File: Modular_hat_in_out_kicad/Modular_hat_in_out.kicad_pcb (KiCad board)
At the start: 2 copper layers, 65 x 56 mm, 147 parts, among them J1 Raspberry_Pi_2_3, U1 MCP3008, U2 LM324, U3 MCP3008, U4 MCP4728, U5 MCP4728, U6 LM324

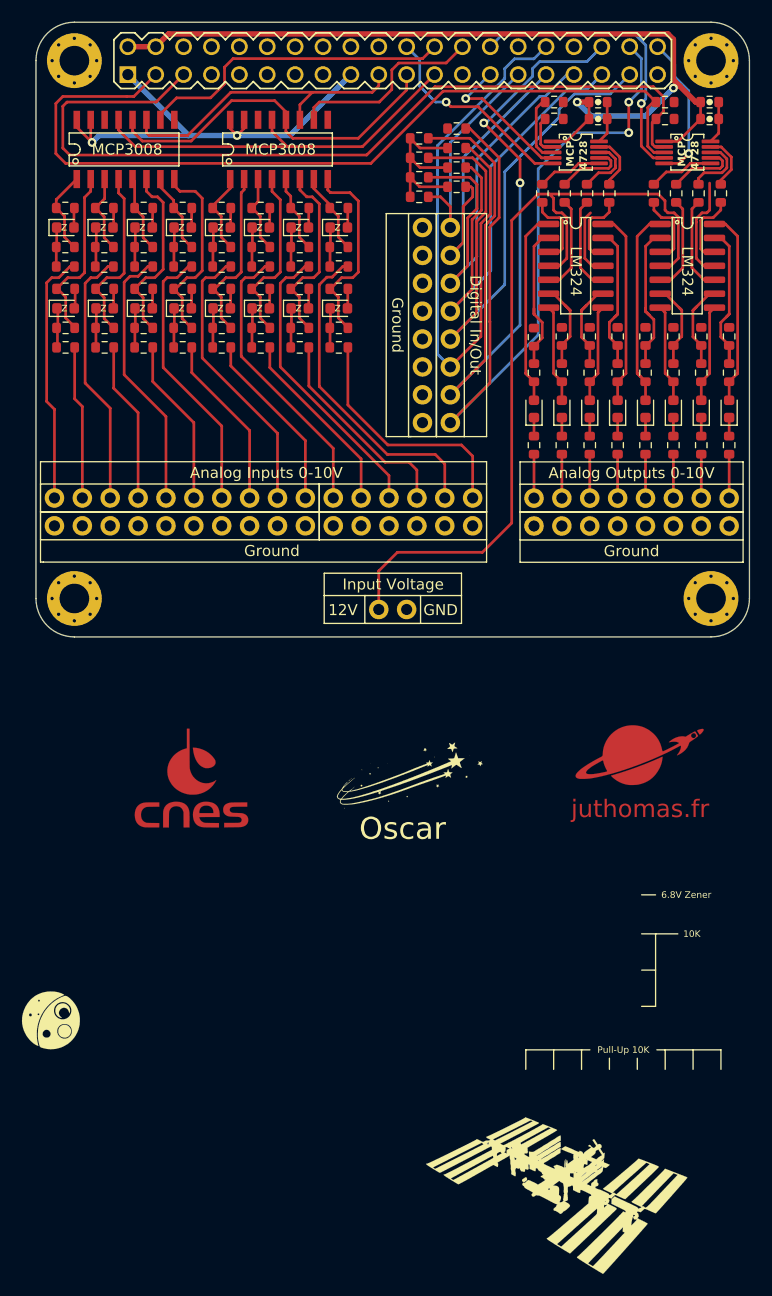
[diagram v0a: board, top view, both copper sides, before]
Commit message: [ADD] Some routing
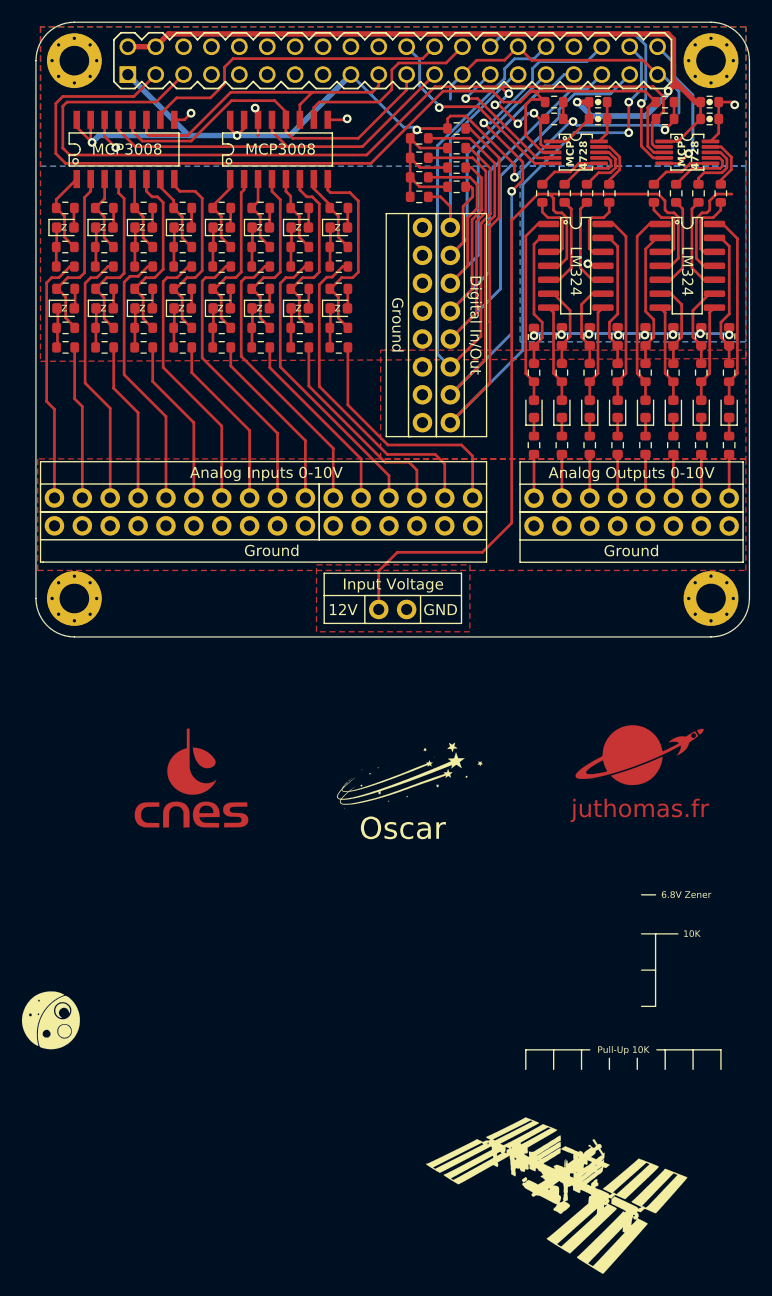
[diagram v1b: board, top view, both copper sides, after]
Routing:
- net GND: track 52.0 -> 109.7 mm, vias 0 -> 14
- net /3V3_REG: track 58.8 -> 102.4 mm, vias 2 -> 6
- net /GPIO3: track 83.5 -> 92.7 mm, vias 0 -> 4
- net /GPIO2: track 85.6 -> 89.6 mm
- net Net-(U6-In4N): track 15.0 -> 13.0 mm
- net Net-(U6-In1N): track 13.8 -> 12.8 mm
- net Net-(U2-In2N): track 8.40 -> 7.75 mm
- added copper zone on B.Cu, net GND
- added copper zone on F.Cu, net GND

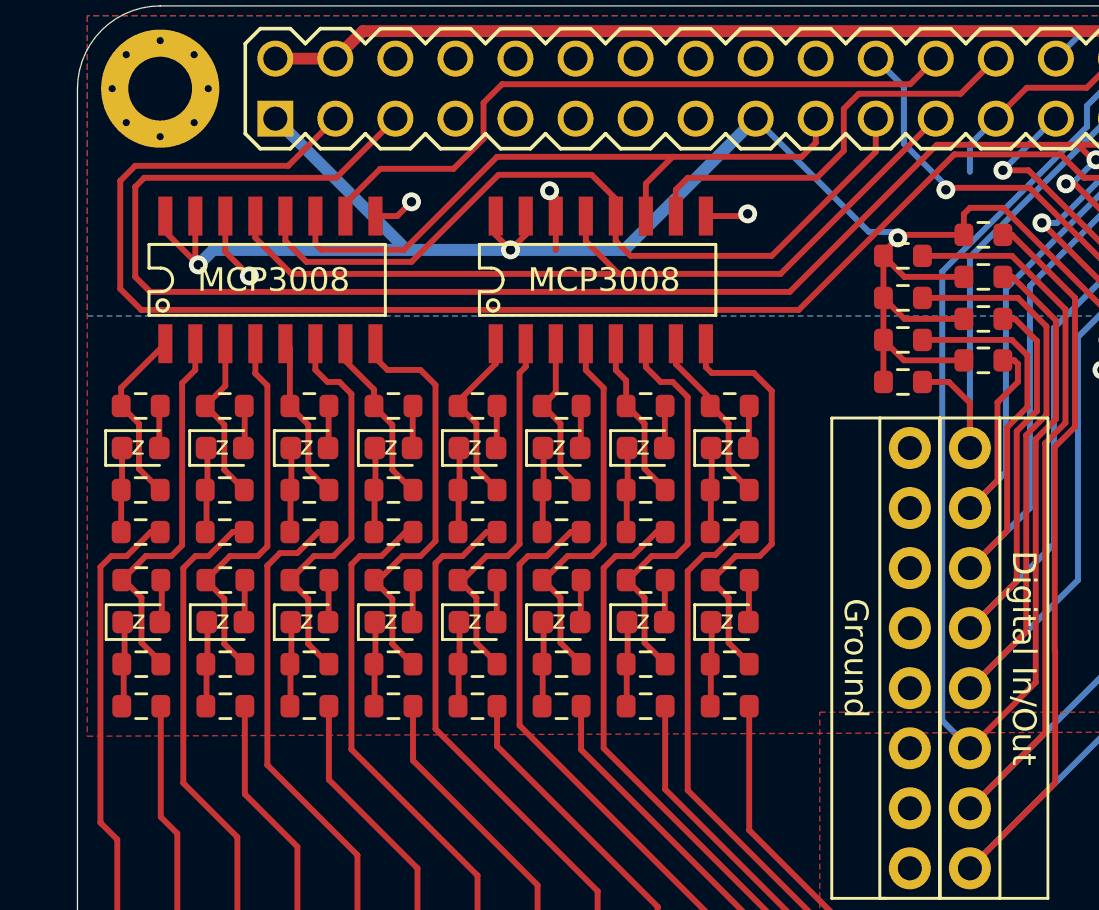
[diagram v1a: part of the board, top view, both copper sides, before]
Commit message: [ADD] Some GND routing
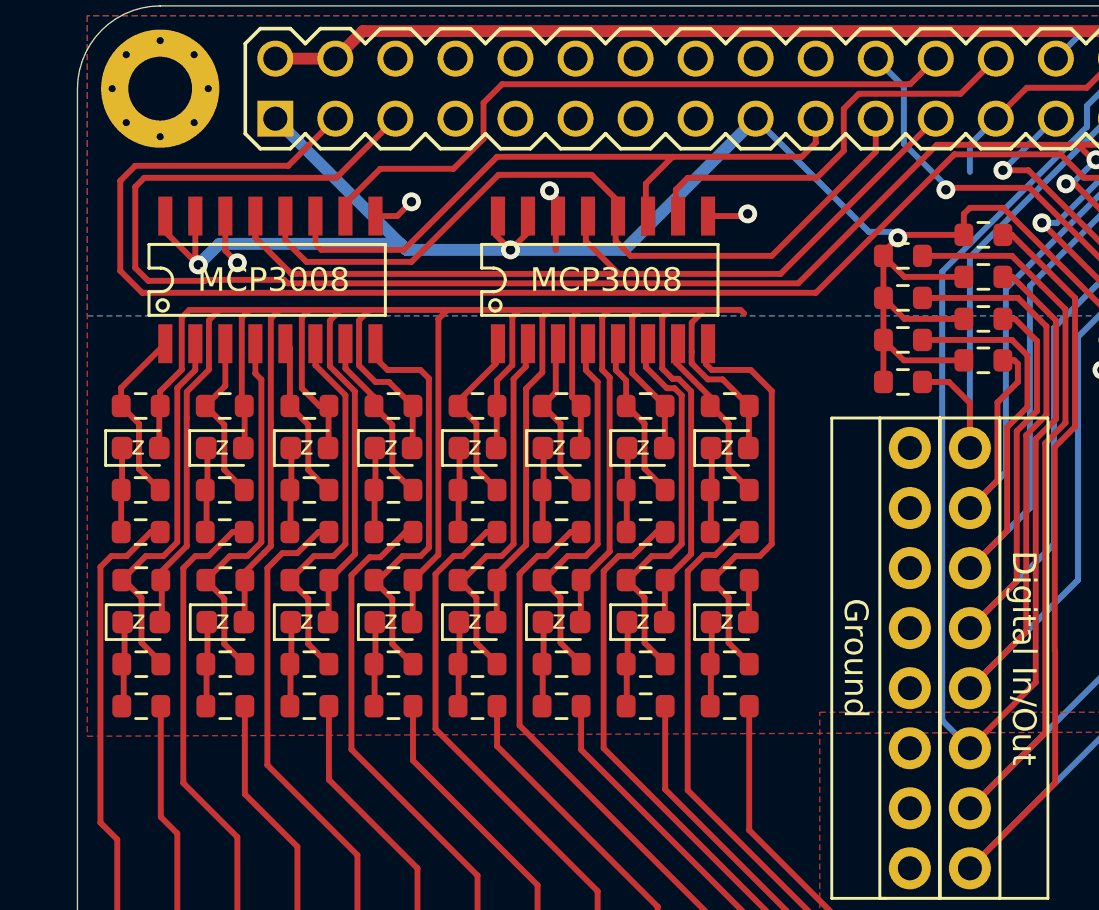
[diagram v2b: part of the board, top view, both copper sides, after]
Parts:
- moved U3 0.09 mm to (47.1, 36.8)
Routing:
- net GND: track 109.7 -> 257.2 mm
- net /GPIO2: track 89.6 -> 88.6 mm
- net /CH5: track 16.7 -> 16.2 mm

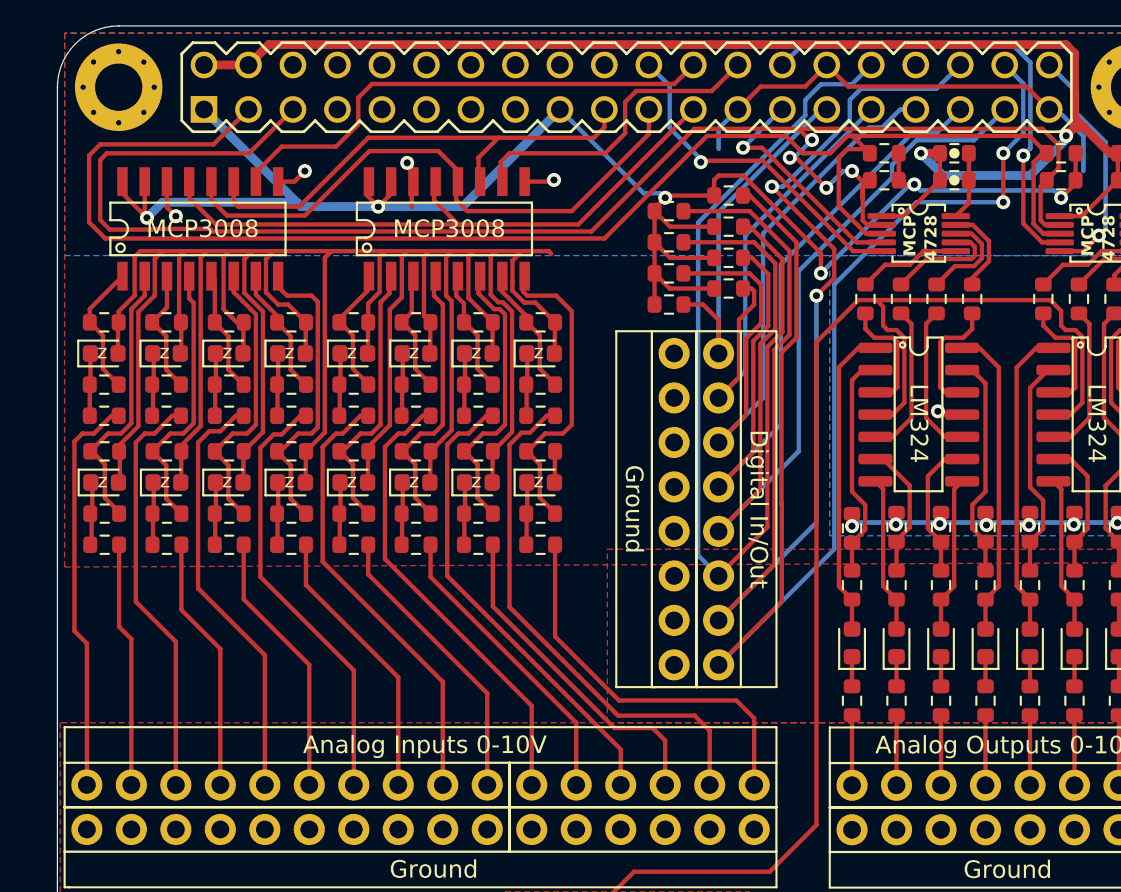
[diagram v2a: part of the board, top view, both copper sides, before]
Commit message: [ADD] ERC & DRC OK
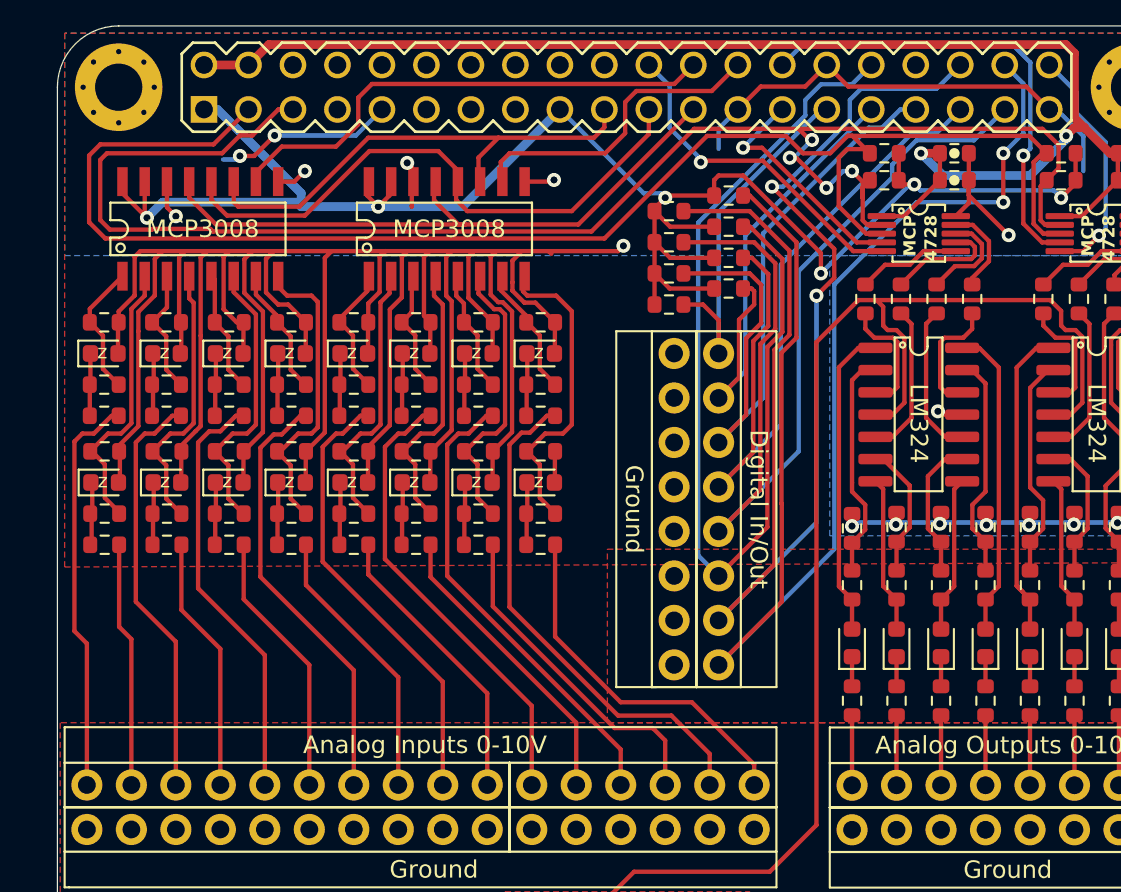
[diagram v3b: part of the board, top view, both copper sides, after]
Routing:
- net GND: track 257.2 -> 275.9 mm, vias 14 -> 18
- net /RG15: track 22.4 -> 20.8 mm
- net /RG14: track 30.0 -> 29.2 mm

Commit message: [ADD] Some Silkcreen
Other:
- board text added: "."
- board text added: "0"
- board text added: "1"
- board text added: "100V"
- board text added: "10K Pull-Up"
- board text added: "48K"
- board text added: "750R"
- board text added: "u"

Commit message: [ADD] Some pigeons
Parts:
- added REF**: Pigeon-3, Modular Shield:Pigeon-3, F.Cu at (41.5, 59.4)
- added REF**: Pigeon-1, Modular Shield:Pigeon-1, F.Cu at (32.4, 60.5)
- added REF**: Pigeon-2, Modular Shield:Pigeon-2, F.Cu at (51.6, 60.5)
